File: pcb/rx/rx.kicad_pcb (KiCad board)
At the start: 2 copper layers, 2 parts, among them U1 MCP33151-05-E/MS, U2 NCS20162DR2G

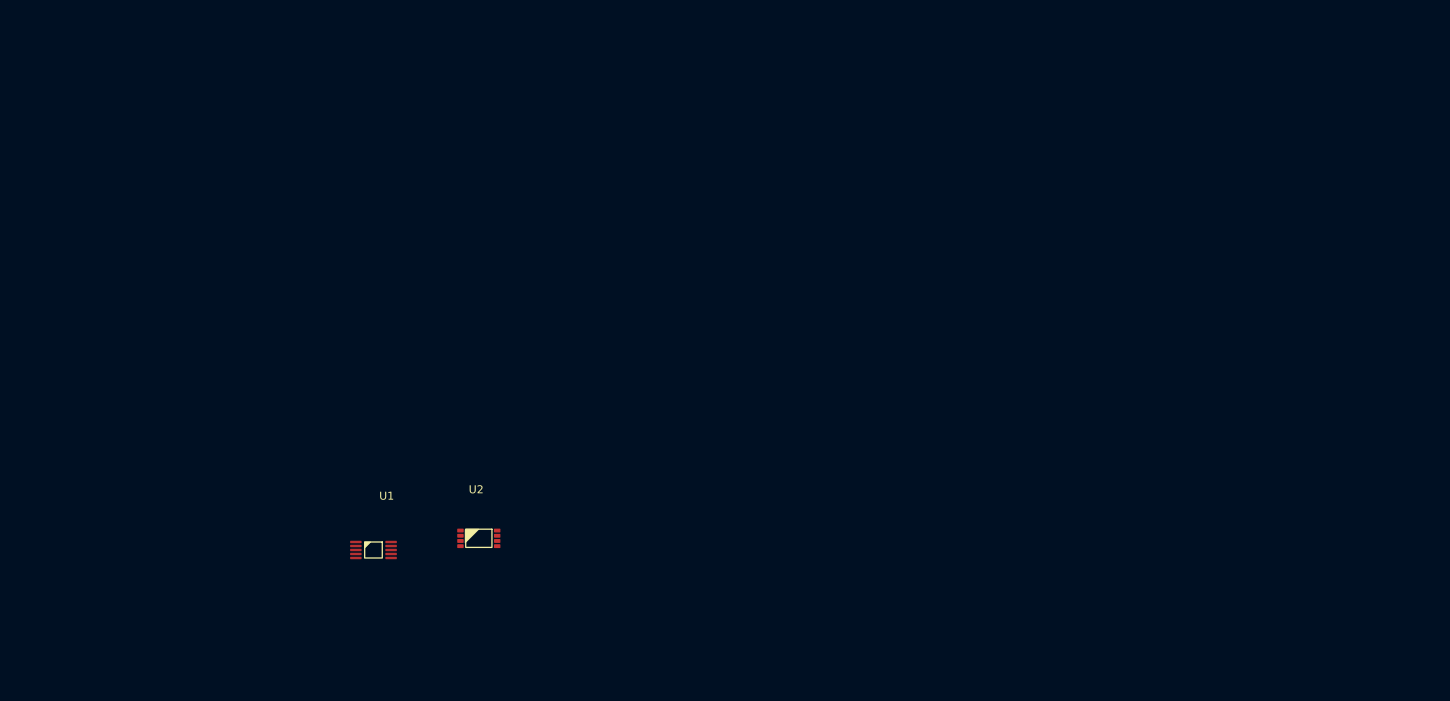
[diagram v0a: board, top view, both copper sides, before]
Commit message: Update perfboard prototype front end
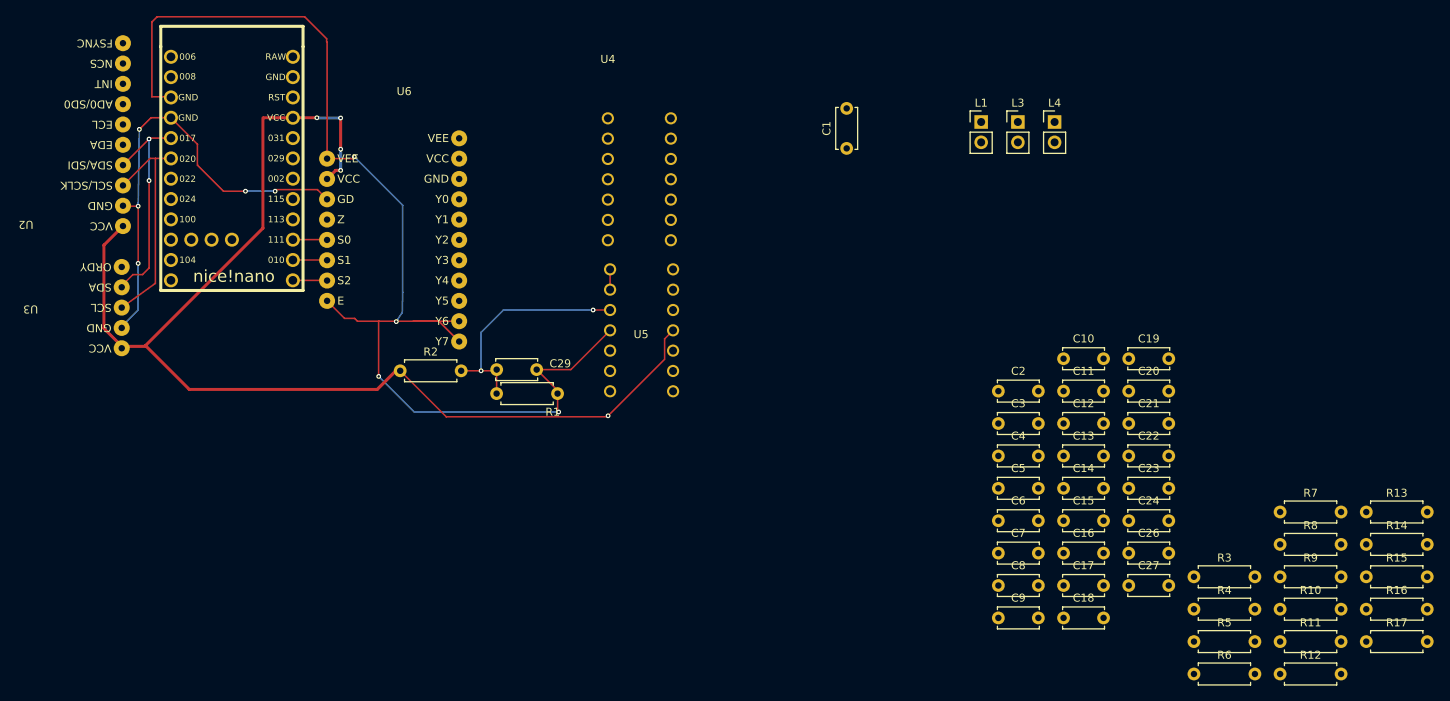
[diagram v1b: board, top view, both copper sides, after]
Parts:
- added C1: 33nF, Capacitor_THT:C_Disc_D5.0mm_W2.5mm_P5.00mm, F.Cu at (179.4, 38.3)
- added C10: 330pF, Capacitor_THT:C_Disc_D5.0mm_W2.5mm_P5.00mm, F.Cu at (206.6, 64.6)
- added C11: 0.1uF, Capacitor_THT:C_Disc_D5.0mm_W2.5mm_P5.00mm, F.Cu at (206.6, 68.6)
- added C12: 330pF, Capacitor_THT:C_Disc_D5.0mm_W2.5mm_P5.00mm, F.Cu at (206.6, 72.7)
- added C13: 100nF, Capacitor_THT:C_Disc_D5.0mm_W2.5mm_P5.00mm, F.Cu at (206.6, 76.7)
- added C14: 1nF, Capacitor_THT:C_Disc_D5.0mm_W2.5mm_P5.00mm, F.Cu at (206.6, 80.8)
- added C15: 10nF, Capacitor_THT:C_Disc_D5.0mm_W2.5mm_P5.00mm, F.Cu at (206.6, 84.8)
- added C16: 47nF, Capacitor_THT:C_Disc_D5.0mm_W2.5mm_P5.00mm, F.Cu at (206.6, 88.9)
- added C17: 330pF, Capacitor_THT:C_Disc_D5.0mm_W2.5mm_P5.00mm, F.Cu at (206.6, 92.9)
- added C18: 0.1uF, Capacitor_THT:C_Disc_D5.0mm_W2.5mm_P5.00mm, F.Cu at (206.6, 97.0)
- added C19: 330pF, Capacitor_THT:C_Disc_D5.0mm_W2.5mm_P5.00mm, F.Cu at (214.7, 64.6)
- added C2: 47nF, Capacitor_THT:C_Disc_D5.0mm_W2.5mm_P5.00mm, F.Cu at (198.4, 68.6)
- added C20: 100nF, Capacitor_THT:C_Disc_D5.0mm_W2.5mm_P5.00mm, F.Cu at (214.7, 68.6)
- added C21: 1nF, Capacitor_THT:C_Disc_D5.0mm_W2.5mm_P5.00mm, F.Cu at (214.7, 72.7)
- added C22: 2.2nf, Capacitor_THT:C_Disc_D5.0mm_W2.5mm_P5.00mm, F.Cu at (214.7, 76.7)
- added C23: 2.2nF, Capacitor_THT:C_Disc_D5.0mm_W2.5mm_P5.00mm, F.Cu at (214.7, 80.8)
- added C24: 2.2nF, Capacitor_THT:C_Disc_D5.0mm_W2.5mm_P5.00mm, F.Cu at (214.7, 84.8)
- added C26: 0.1uF, Capacitor_THT:C_Disc_D5.0mm_W2.5mm_P5.00mm, F.Cu at (214.7, 88.9)
- added C27: 0.1uF, Capacitor_THT:C_Disc_D5.0mm_W2.5mm_P5.00mm, F.Cu at (214.7, 92.9)
- added C29: 0.1uF, Capacitor_THT:C_Disc_D5.0mm_W2.5mm_P5.00mm, F.Cu at (140.7, 66.0)
- added C3: 330pF, Capacitor_THT:C_Disc_D5.0mm_W2.5mm_P5.00mm, F.Cu at (198.4, 72.7)
- added C4: 0.1uF, Capacitor_THT:C_Disc_D5.0mm_W2.5mm_P5.00mm, F.Cu at (198.4, 76.7)
- added C5: 100nF, Capacitor_THT:C_Disc_D5.0mm_W2.5mm_P5.00mm, F.Cu at (198.4, 80.8)
- added C6: 330pF, Capacitor_THT:C_Disc_D5.0mm_W2.5mm_P5.00mm, F.Cu at (198.4, 84.8)
- added C7: 1nF, Capacitor_THT:C_Disc_D5.0mm_W2.5mm_P5.00mm, F.Cu at (198.4, 88.9)
- added C8: 10nF, Capacitor_THT:C_Disc_D5.0mm_W2.5mm_P5.00mm, F.Cu at (198.4, 92.9)
- added C9: 47nF, Capacitor_THT:C_Disc_D5.0mm_W2.5mm_P5.00mm, F.Cu at (198.4, 97.0)
- added L1: 0.7mH, Connector_PinHeader_2.54mm:PinHeader_1x02_P2.54mm_Vertical, F.Cu at (196.3, 35.0)
- added L3: 2mH, Connector_PinHeader_2.54mm:PinHeader_1x02_P2.54mm_Vertical, F.Cu at (200.8, 35.0)
- added L4: 2mH, Connector_PinHeader_2.54mm:PinHeader_1x02_P2.54mm_Vertical, F.Cu at (205.4, 35.0)
- added R1: 10K, Resistor_THT:R_Axial_DIN0207_L6.3mm_D2.5mm_P7.62mm_Horizontal, F.Cu at (135.7, 69.0)
- added R10: 750, Resistor_THT:R_Axial_DIN0207_L6.3mm_D2.5mm_P7.62mm_Horizontal, F.Cu at (233.6, 95.9)
- added R11: 6.8K, Resistor_THT:R_Axial_DIN0207_L6.3mm_D2.5mm_P7.62mm_Horizontal, F.Cu at (233.6, 100.0)
- added R12: 2.2K, Resistor_THT:R_Axial_DIN0207_L6.3mm_D2.5mm_P7.62mm_Horizontal, F.Cu at (233.6, 104.0)
- added R13: 750, Resistor_THT:R_Axial_DIN0207_L6.3mm_D2.5mm_P7.62mm_Horizontal, F.Cu at (244.4, 83.8)
- added R14: 6.8K, Resistor_THT:R_Axial_DIN0207_L6.3mm_D2.5mm_P7.62mm_Horizontal, F.Cu at (244.4, 87.8)
- added R15: 750, Resistor_THT:R_Axial_DIN0207_L6.3mm_D2.5mm_P7.62mm_Horizontal, F.Cu at (244.4, 91.8)
- added R16: 6.8K, Resistor_THT:R_Axial_DIN0207_L6.3mm_D2.5mm_P7.62mm_Horizontal, F.Cu at (244.4, 95.9)
- added R17: 2.2K, Resistor_THT:R_Axial_DIN0207_L6.3mm_D2.5mm_P7.62mm_Horizontal, F.Cu at (244.4, 100.0)
- added R2: 10K, Resistor_THT:R_Axial_DIN0207_L6.3mm_D2.5mm_P7.62mm_Horizontal, F.Cu at (123.6, 66.1)
- added R3: 750, Resistor_THT:R_Axial_DIN0207_L6.3mm_D2.5mm_P7.62mm_Horizontal, F.Cu at (222.9, 91.8)
- added R4: 6.8K, Resistor_THT:R_Axial_DIN0207_L6.3mm_D2.5mm_P7.62mm_Horizontal, F.Cu at (222.9, 95.9)
- added R5: 750, Resistor_THT:R_Axial_DIN0207_L6.3mm_D2.5mm_P7.62mm_Horizontal, F.Cu at (222.9, 100.0)
- added R6: 6.8K, Resistor_THT:R_Axial_DIN0207_L6.3mm_D2.5mm_P7.62mm_Horizontal, F.Cu at (222.9, 104.0)
- added R7: 2.2K, Resistor_THT:R_Axial_DIN0207_L6.3mm_D2.5mm_P7.62mm_Horizontal, F.Cu at (233.6, 83.8)
- added R8: 750, Resistor_THT:R_Axial_DIN0207_L6.3mm_D2.5mm_P7.62mm_Horizontal, F.Cu at (233.6, 87.8)
- added R9: 6.8K, Resistor_THT:R_Axial_DIN0207_L6.3mm_D2.5mm_P7.62mm_Horizontal, F.Cu at (233.6, 91.8)
- added U3: QMC5883P, Library:QMC5883P, F.Cu at (90.1, 64.5)
- added U4: MCP6004, Library:MCP6004, F.Cu at (149.6, 32.0)
- added U5: MCP6004, Library:MCP6004, F.Cu at (157.8, 71.2)
- added U6: 74HC4051, Library:74HC4051, F.Cu at (113.2, 34.5)
- U1: value MCP33151-05-E/MS -> nice_nano; footprint custom-lib:MCP33151-05-E_MS -> nice nano:nice_nano
- U2: value NCS20162DR2G -> MPU-6500; footprint custom-lib:NCS20162 -> Library:MPU-6500
- moved U2 72.6 mm to (81.4, 38.3), turned to 180 degrees
- moved U1 50.7 mm to (102.6, 40.8)
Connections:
- U1 pad 3: unconnected-(U1-A_IN+-Pad3) -> GND
- U1 pad 4: unconnected-(U1-A_IN--Pad4) -> GND
- U1 pad 5: unconnected-(U1-GND-Pad5) -> /SDA
- U1 pad 6: unconnected-(U1-CNVST-Pad6) -> /SCK
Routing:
- net GND: track 0.00 -> 207.7 mm, vias 0 -> 9
- net +3.3V: track 0.00 -> 150.9 mm, vias 0 -> 5
- net Net-(U5C-+): track 0.00 -> 29.6 mm, vias 0 -> 2
- net /SCK: track 0.00 -> 28.4 mm
- net /SDA: track 0.00 -> 27.8 mm, vias 0 -> 2
- net /SELECT_2: track 0.00 -> 4.29 mm
- net /SELECT_1: track 0.00 -> 4.29 mm
- net /SELECT_0: track 0.00 -> 4.29 mm
- net /V_BIAS: track 0.00 -> 2.54 mm

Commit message: Created rx board for order
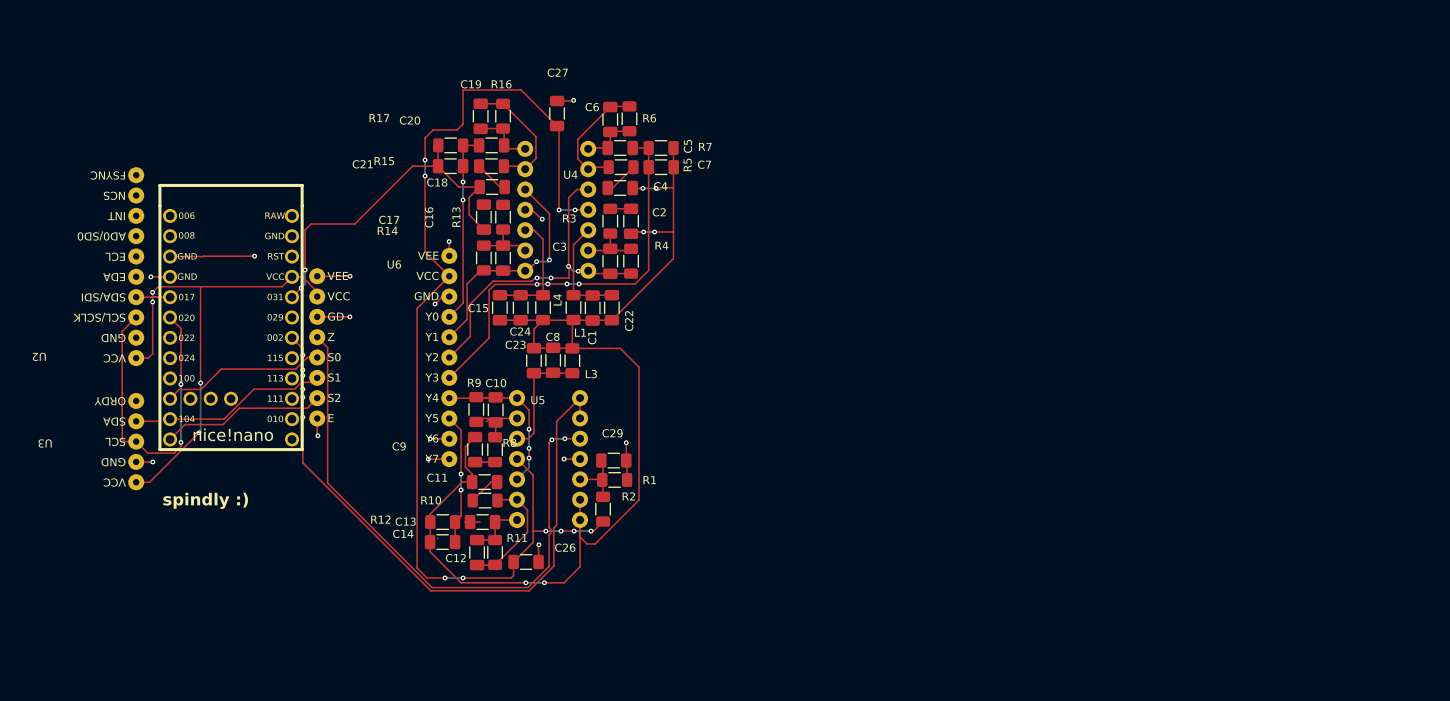
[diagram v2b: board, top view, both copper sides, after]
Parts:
- C1, C10, C11, C12, C13, C14, C15, C16, C17, C18, C19, C2, C20, C21, C22, C23, C24, C26, C27, C29, C3, C4, C5, C6, C7, C8, C9: footprint Capacitor_THT:C_Disc_D5.0mm_W2.5mm_P5.00mm -> Capacitor_SMD:C_1206_3216Metric_Pad1.33x1.80mm_HandSolder
- L1, L3, L4: footprint Connector_PinHeader_2.54mm:PinHeader_1x02_P2.54mm_Vertical -> Resistor_SMD:R_1206_3216Metric_Pad1.30x1.75mm_HandSolder
- R1, R10, R11, R12, R13, R14, R15, R16, R17, R2, R3, R4, R5, R6, R7, R8, R9: footprint Resistor_THT:R_Axial_DIN0207_L6.3mm_D2.5mm_P7.62mm_Horizontal -> Resistor_SMD:R_1206_3216Metric_Pad1.30x1.75mm_HandSolder
- moved R17 130.2 mm to (129.9, 37.9), turned to 180 degrees
- moved R16 124.3 mm to (136.5, 34.3), turned to 90 degrees
- moved R15 120.8 mm to (135.1, 40.5), turned to 180 degrees
- moved R14 116.0 mm to (134.1, 52.0), turned to 90 degrees
- moved R13 114.0 mm to (136.5, 46.9), turned to 90 degrees
- moved R12 106.4 mm to (128.9, 85.0), turned to 180 degrees
- moved R9 102.6 mm to (133.2, 70.9), turned to -90 degrees
- moved R10 100.3 mm to (134.2, 82.3), turned to 180 degrees
- moved R6 99.0 mm to (152.3, 34.6), turned to 90 degrees
- moved R8 98.8 mm to (135.5, 76.0), turned to -90 degrees
- moved R11 98.8 mm to (135.5, 88.8), turned to -90 degrees
- moved R5 93.0 mm to (151.2, 40.6)
- moved C27 92.7 mm to (143.2, 33.9), turned to 90 degrees
- moved C21 90.7 mm to (129.9, 40.5)
- moved R7 89.8 mm to (156.2, 38.2)
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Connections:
- U1 pad 10: unconnected-(U1-P0.11-Pad10) -> /SELECT_0
- U1 pad 11: unconnected-(U1-P1.04-Pad11) -> /SELECT_1
- U1 pad 12: unconnected-(U1-P1.06-Pad12) -> /SELECT_2
- U1 pad 13: /SELECT_2 -> unconnected-(U1-NFC1/P0.09-Pad13)
- U1 pad 14: /SELECT_1 -> unconnected-(U1-NFC2/P0.10-Pad14)
- U1 pad 15: /SELECT_0 -> unconnected-(U1-P1.11-Pad15)
- U1 pad 20: unconnected-(U1-AIN7/P0.31-Pad20) -> /V_BIAS
- U6 pad 12: /V_OUT3 -> /V_OUT4
- U6 pad 15: /V_OUT4 -> /V_OUT3
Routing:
- net /V_BIAS: track 2.54 -> 191.9 mm, vias 0 -> 8
- net GND: track 207.7 -> 48.9 mm, vias 9 -> 15
- net /ADC_0: track 0.00 -> 80.4 mm, vias 0 -> 6
- net /ADC_BUFFER: track 0.00 -> 72.7 mm, vias 0 -> 2
- net /V_OUT4: track 0.00 -> 51.3 mm, vias 0 -> 4
- net +3.3V: track 150.9 -> 194.1 mm, vias 5 -> 14
- net /V_OUT3: track 0.00 -> 42.6 mm, vias 0 -> 4
- net /V_OUT1: track 0.00 -> 29.2 mm, vias 0 -> 2
- net /V_OUT2: track 0.00 -> 24.1 mm, vias 0 -> 2
- net Net-(U5C-+): track 29.6 -> 7.43 mm, vias 2 -> 0
- net /V_OUT5: track 0.00 -> 20.0 mm, vias 0 -> 3
- net /V_OUT6: track 0.00 -> 18.4 mm, vias 0 -> 2
- net /SELECT_0: track 4.29 -> 20.6 mm
- net /SELECT_2: track 4.29 -> 20.5 mm
- net /SELECT_1: track 4.29 -> 20.5 mm
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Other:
- board text added: "spindly :)"

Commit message: Finished Rx
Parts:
- added BT1: Battery, Connector_JST:JST_PH_B2B-PH-K_1x02_P2.00mm_Vertical, F.Cu at (118.5, 35.6)
- added G***: LOGO, Library:cat_silkscreen, F.Cu at (98.3, 83.4)
- added REF**: MountingHole_3.2mm_M3_Pad, MountingHole:MountingHole_3.2mm_M3_Pad, F.Cu at (158.0, 31.5)
- added REF**: MountingHole_3.2mm_M3_Pad, MountingHole:MountingHole_3.2mm_M3_Pad, F.Cu at (86.0, 89.5)
- added REF**: MountingHole_3.2mm_M3_Pad, MountingHole:MountingHole_3.2mm_M3_Pad, F.Cu at (86.0, 31.5)
- added REF**: MountingHole_3.2mm_M3_Pad, MountingHole:MountingHole_3.2mm_M3_Pad, F.Cu at (158.0, 89.5)
- added SW1: SW_SPDT, Library:EG1218, F.Cu at (121.5, 41.7)
- moved R11 0.10 mm to (135.6, 88.8)
- moved C6 0.09 mm to (149.9, 34.6)
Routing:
- net /ADC_0: track 80.4 -> 111.4 mm, vias 6 -> 8
- net /B-: track 0.00 -> 25.1 mm
- net /V_BIAS: track 191.9 -> 214.7 mm, vias 8 -> 14
- net /B+: track 0.00 -> 15.2 mm
- net +3.3V: track 194.1 -> 207.2 mm
- net Net-(BT1-+): track 0.00 -> 5.13 mm
- net Net-(C16-Pad1): track 0.00 -> 2.41 mm
- net Net-(U5A--): track 7.17 -> 6.55 mm
- added copper zone on B.Cu, net GND
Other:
- board outline added: 82.3 x 70.8 mm
- board text added: "prototype 0"
